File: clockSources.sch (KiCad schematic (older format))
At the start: 0 parts

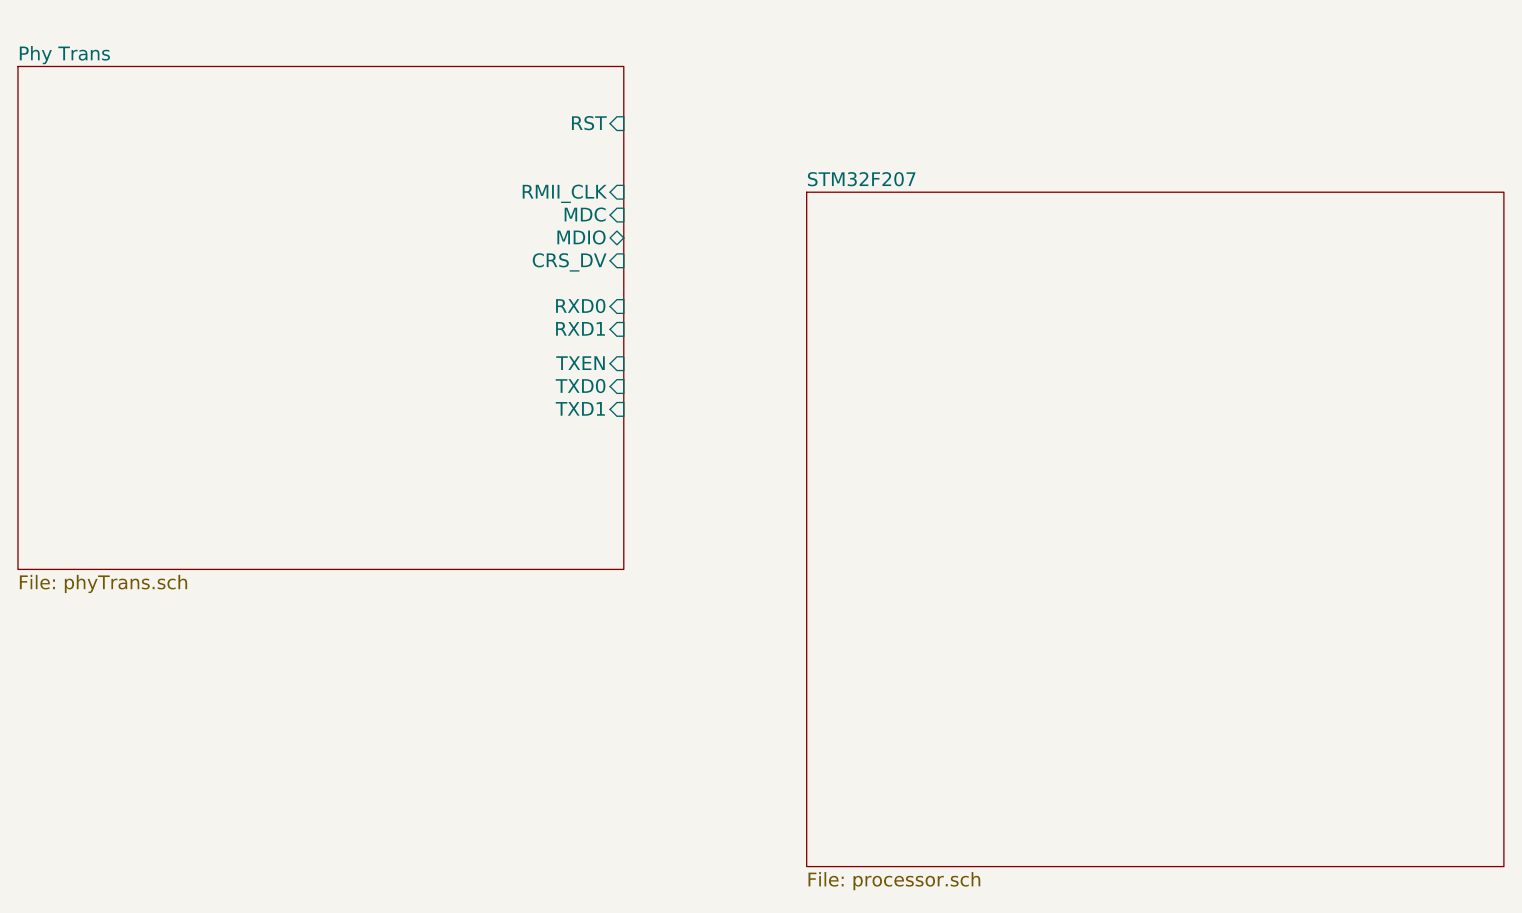
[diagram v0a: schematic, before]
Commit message: Made quite a few changes... The Eth Phy and RJ-45 connection should be close to finished. Figured out how to make the hierarchical sheets work.
Need to move the power schematic to a hierarchical sheet.
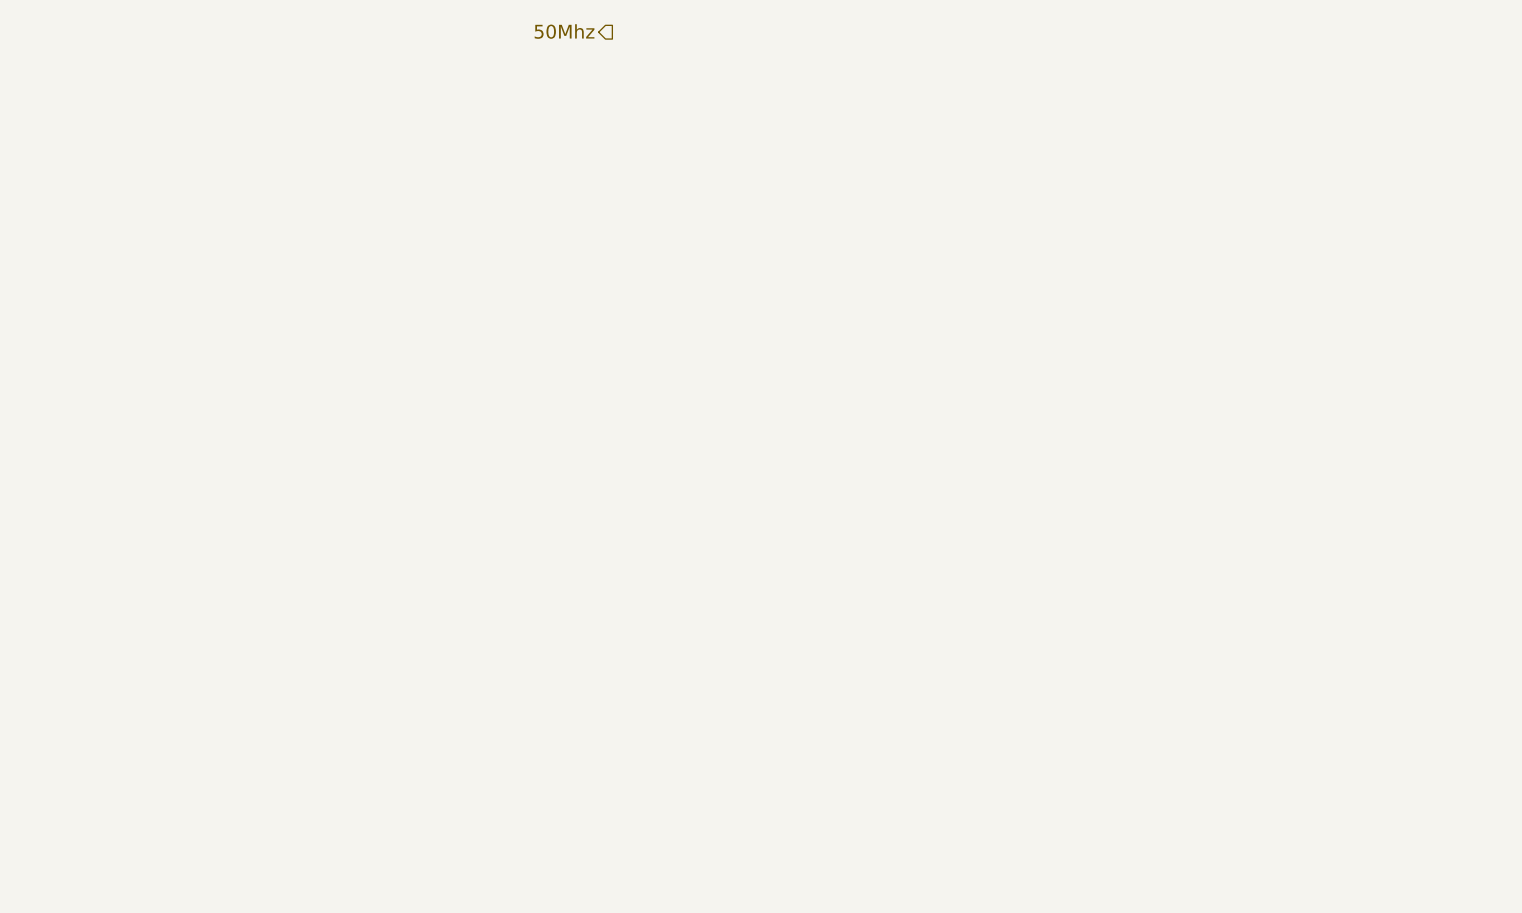
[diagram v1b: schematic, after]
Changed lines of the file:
@@
 $Descr A4 11700 8267
 encoding utf-8
-Sheet 1 5
+Sheet 3 5
 Title ""
 Date "24 sep 2011"
@@
 Comment4 ""
 $EndDescr
-$Sheet
-S 1600 1500 2650 2200
-U 4E7A8C23
-F0 "Phy Trans" 60
-F1 "phyTrans.sch" 60
-F2 "CRS_DV" I R 4250 2350 60
-F3 "RXD1" I R 4250 2650 60
-F4 "RXD0" I R 4250 2550 60
-F5 "TXD1" I R 4250 3000 60
-F6 "TXD0" I R 4250 2900 60
-F7 "TXEN" I R 4250 2800 60
-F8 "RST" I R 4250 1750 60
-F9 "RMII_CLK" I R 4250 2050 60
-F10 "MDC" I R 4250 2150 60
-F11 "MDIO" B R 4250 2250 60
-$EndSheet
-$Sheet
-S 5050 2050 3050 2950
-U 4E7DF058
-F0 "STM32F207" 60
-F1 "processor.sch" 60
-$EndSheet
+Text HLabel 4200 1350 0    60   Output ~ 0
+50Mhz
 $EndSCHEMATC
